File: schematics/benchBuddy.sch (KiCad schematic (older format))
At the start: 0 parts

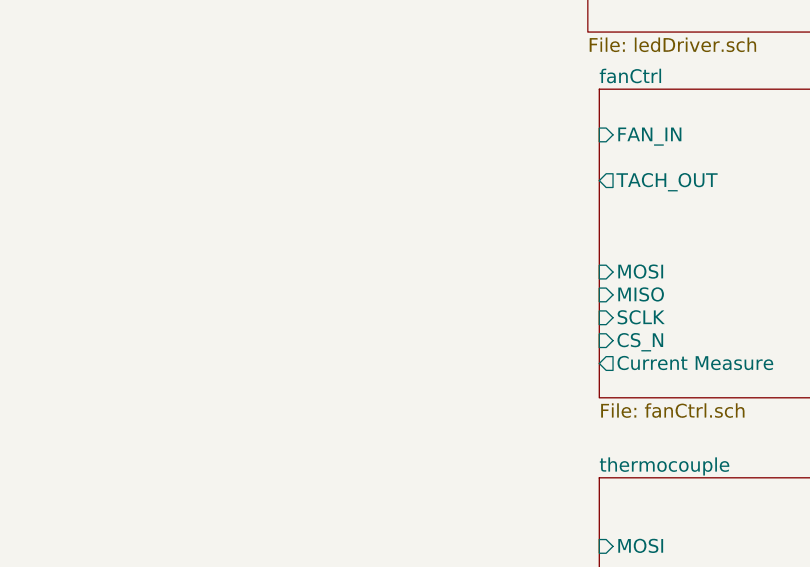
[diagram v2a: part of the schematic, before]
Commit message: added filtering to power
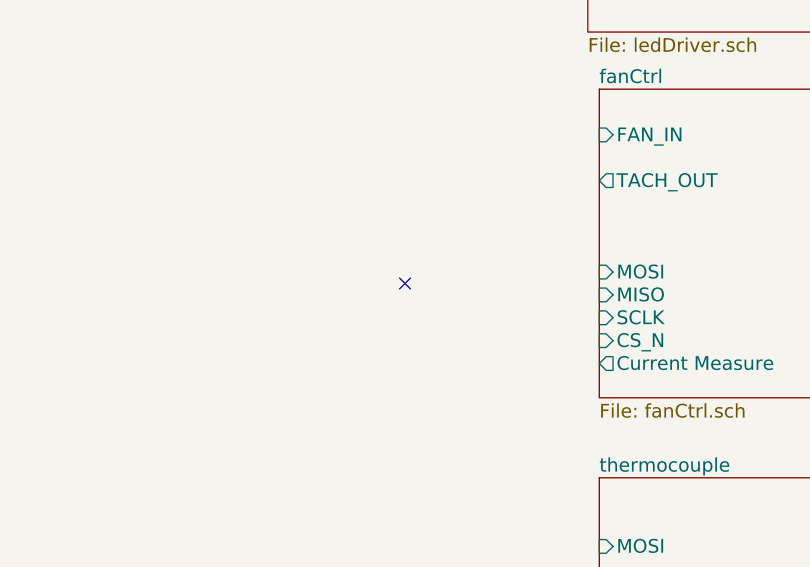
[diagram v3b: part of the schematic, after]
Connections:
- no-connect marks 0 -> 1
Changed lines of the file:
@@
-EESchema Schematic File Version 2  date Tue 08 Oct 2013 10:41:11 PM EDT
+EESchema Schematic File Version 2  date Tue 08 Oct 2013 10:54:15 PM EDT
 LIBS:power
 LIBS:power_addon
@@
 Comment4 ""
 $EndDescr
+NoConn ~ 6500 3450
 $Sheet
 S 4700 750  1850 1200
